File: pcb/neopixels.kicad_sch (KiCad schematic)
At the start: 44 parts

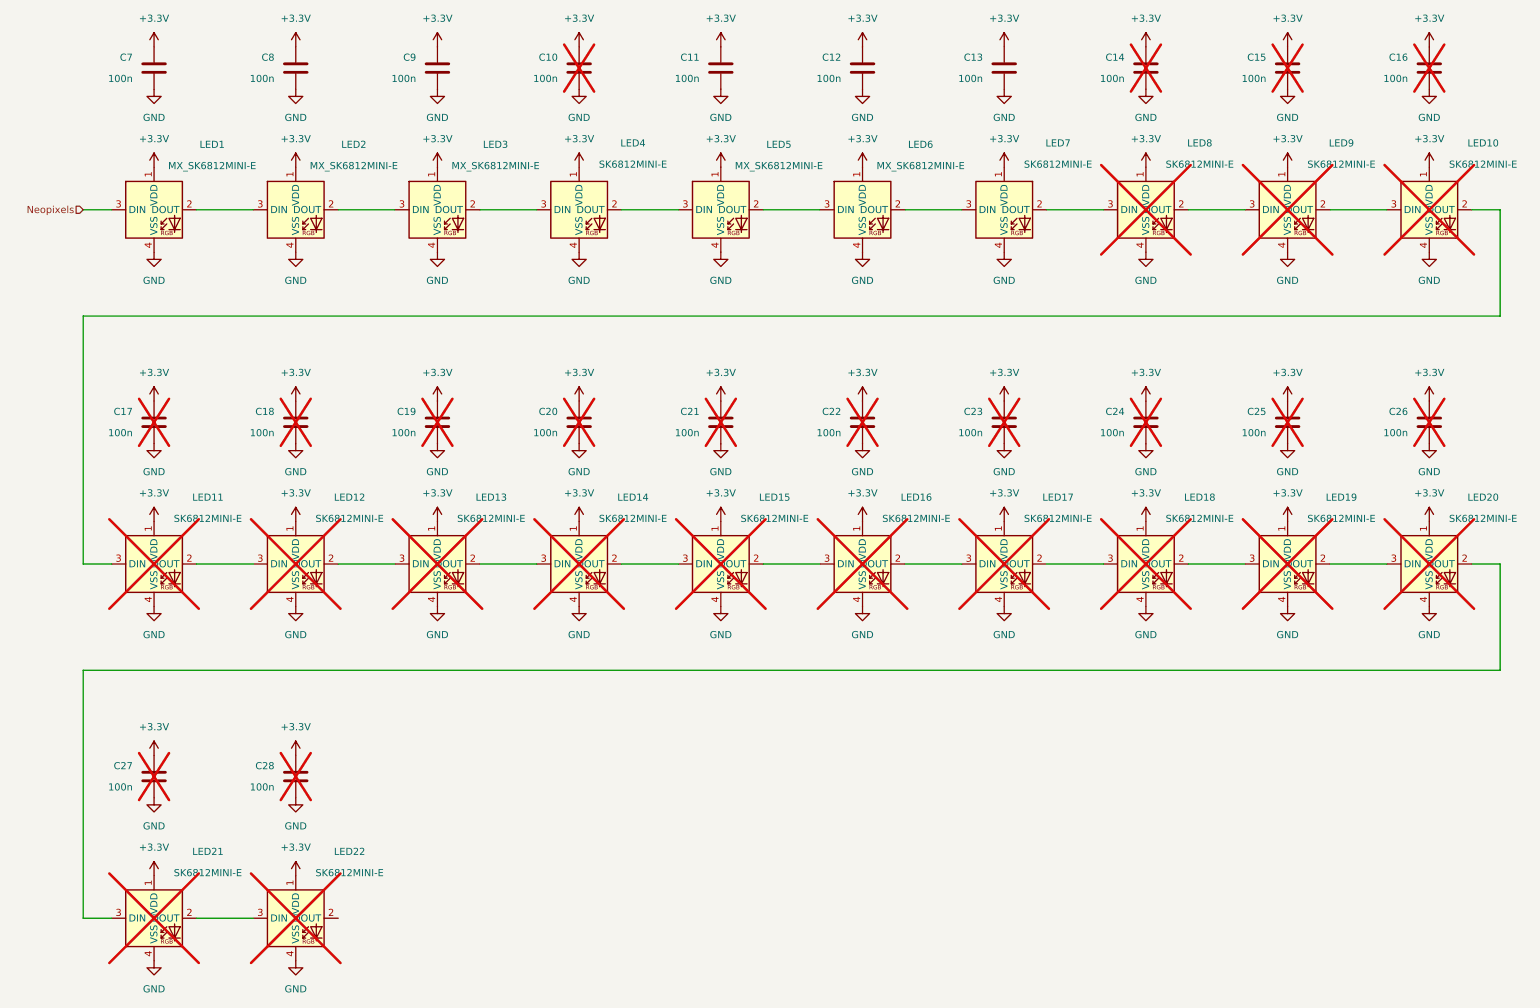
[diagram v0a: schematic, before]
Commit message: add smart power saving circuit + update readme
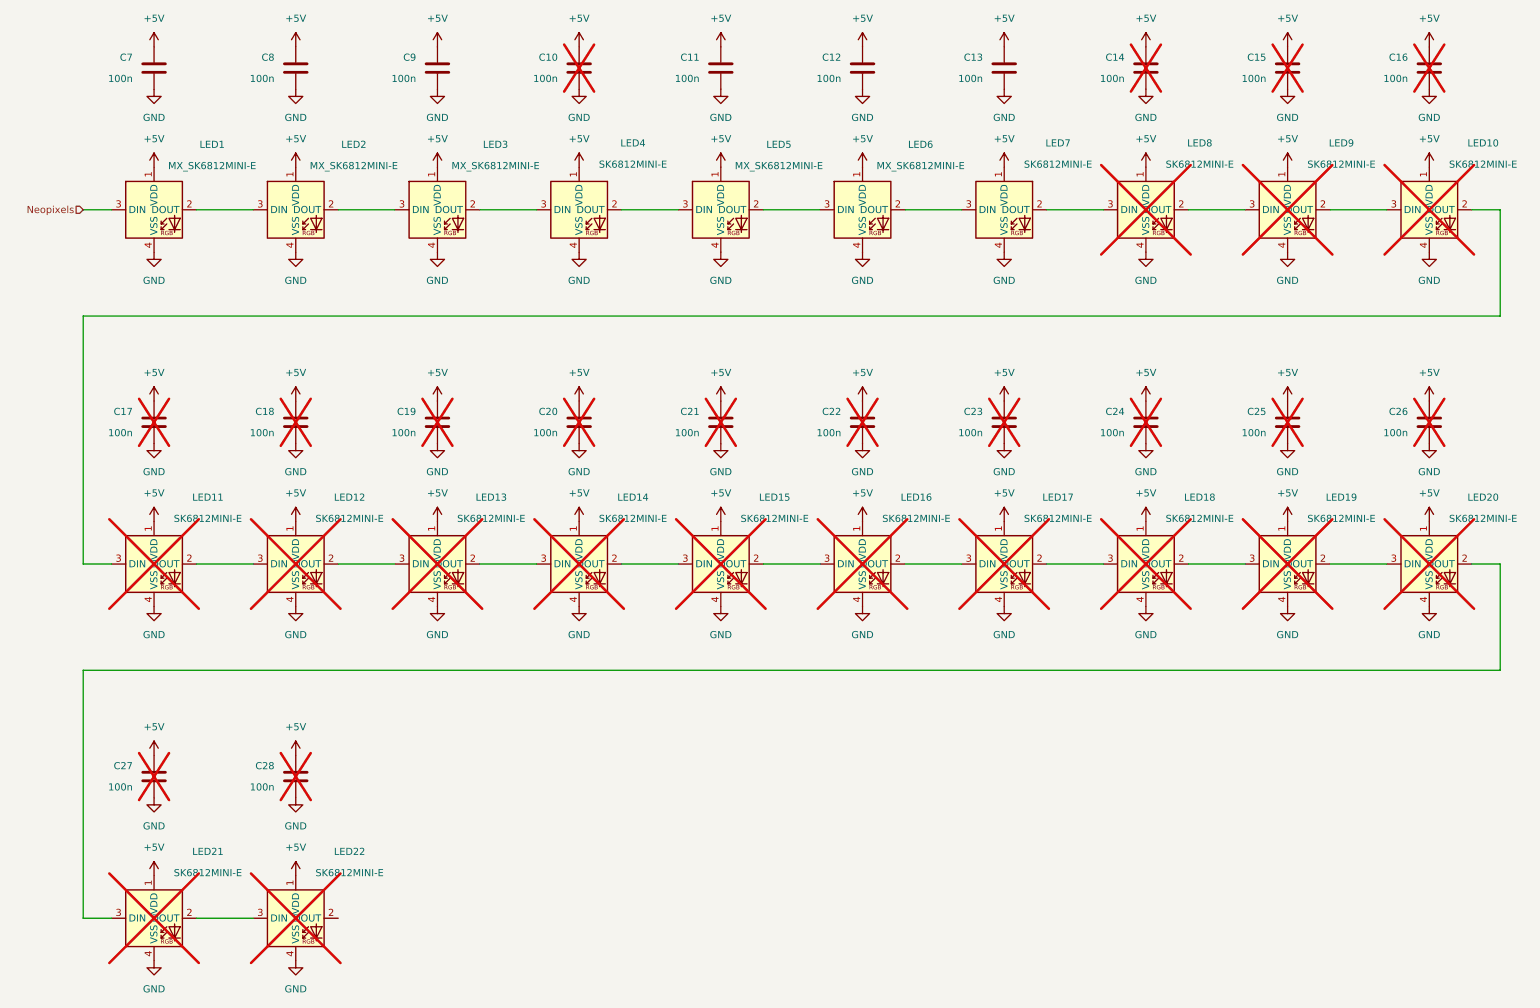
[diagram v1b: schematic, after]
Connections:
- net +3.3V renamed +5V
